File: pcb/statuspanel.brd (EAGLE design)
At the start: 57.1 x 66 mm, 5 parts

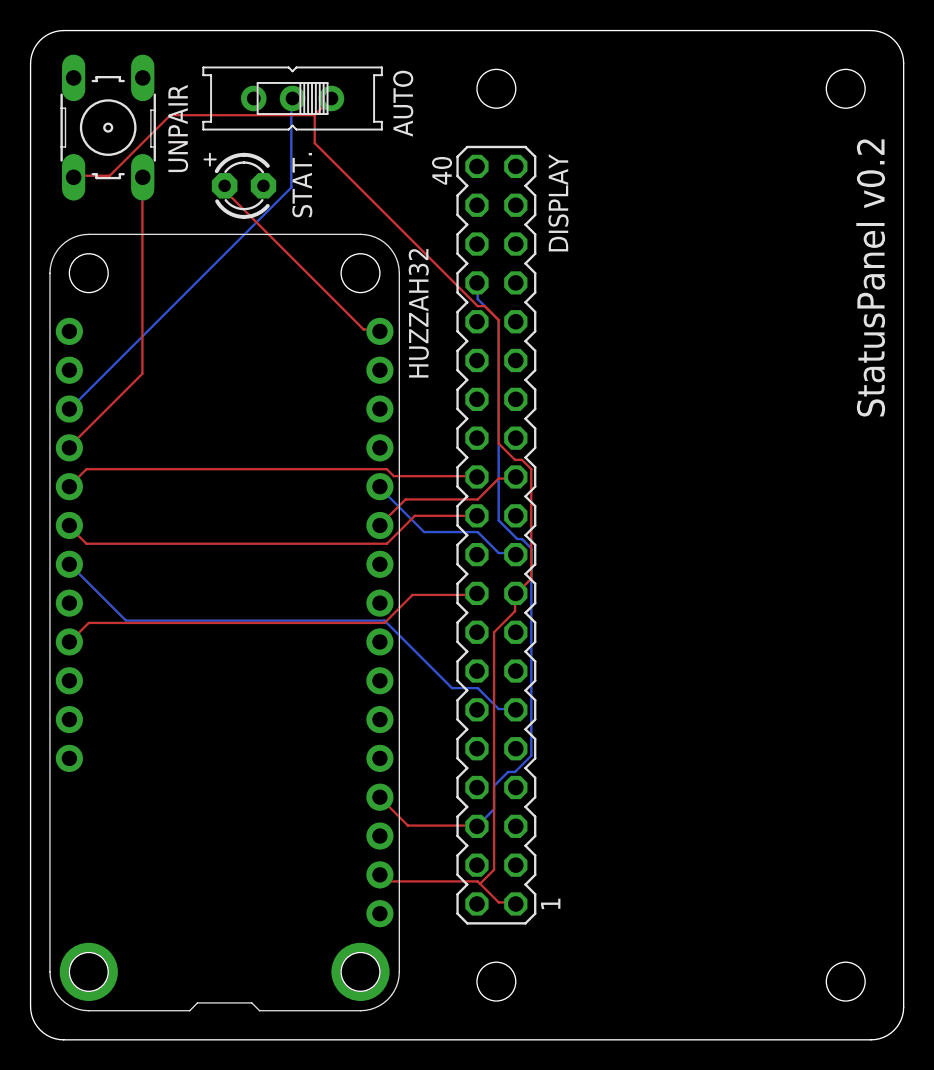
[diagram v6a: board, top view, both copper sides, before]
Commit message: Add the resistors to the board
- Divider
- Status LED
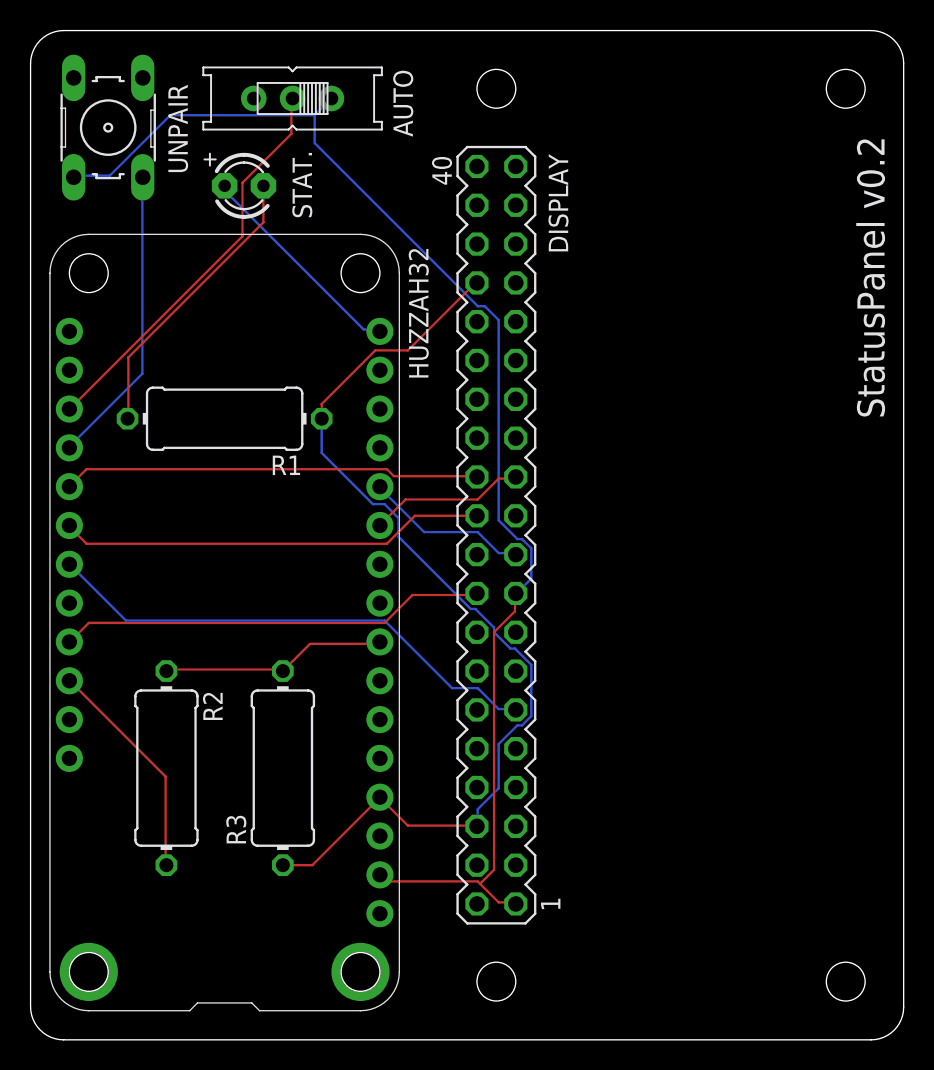
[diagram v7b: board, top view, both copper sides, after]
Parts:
- added R1: 5.1, adafruit:0411/12
- added R2, R3: 4.7K, adafruit:0411/12
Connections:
- new net USB: HUZZAH32.26, R2.2
- new net USBDETECT: HUZZAH32.8, R2.1, R3.2
- net GND: now also R1.1, R3.1
- net N$3: now also R1.2
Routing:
- net N$3: track 0.00 -> 18.9 mm
- net GND: track 46.1 -> 64.5 mm
- net USBDETECT: track 0.00 -> 14.9 mm
- net USB: track 0.00 -> 14.7 mm

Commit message: Update the PCB to tie 5V and 3V3 together to account for the new display controller board.
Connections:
- net 3V3: now also DISPLAY.2, DISPLAY.4
- net GND: now also DISPLAY.14, DISPLAY.20, DISPLAY.25, DISPLAY.30, DISPLAY.9
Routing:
- net GND: track 64.5 -> 81.1 mm
- net 3V3: track 86.8 -> 89.1 mm
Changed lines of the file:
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@@
 <?xml version="1.0" encoding="utf-8"?>
 <!DOCTYPE eagle SYSTEM "eagle.dtd">
-<eagle version="9.5.2">
+<eagle version="9.6.2">
 <drawing>
 <settings>
@@
 <wire x1="30.6324" y1="8.9916" x2="31.6992" y2="8.9916" width="0.1524" layer="1"/>
 <wire x1="29.2608" y1="10.3632" x2="29.4132" y2="10.2108" width="0.1524" layer="1"/>
-<wire x1="29.4132" y1="10.2108" x2="30.6324" y2="8.9916" width="0.1524" layer="1"/>
-<wire x1="23.1648" y1="10.3632" x2="29.2608" y2="10.3632" width="0.1524" layer="1"/>
+<wire x1="29.4132" y1="10.2108" x2="29.8704" y2="9.7536" width="0.1524" layer="1"/>
+<wire x1="29.8704" y1="9.7536" x2="30.6324" y2="8.9916" width="0.1524" layer="1"/>
+<wire x1="23.1648" y1="10.3632" x2="29.1084" y2="10.3632" width="0.1524" layer="1"/>
+<wire x1="29.1084" y1="10.3632" x2="29.2608" y2="10.3632" width="0.1524" layer="1"/>
 <wire x1="22.86" y1="10.668" x2="23.1648" y2="10.3632" width="0.1524" layer="1"/>
 <wire x1="31.6992" y1="8.9916" x2="31.75" y2="8.89" width="0.1524" layer="1"/>
@@
 <wire x1="31.8516" y1="29.2608" x2="32.766" y2="30.1752" width="0.1524" layer="16"/>
 <wire x1="31.8516" y1="29.2608" x2="31.75" y2="29.21" width="0.1524" layer="16"/>
+<contactref element="DISPLAY" pad="4"/>
+<contactref element="DISPLAY" pad="2"/>
+<wire x1="29.8704" y1="9.6012" x2="29.2608" y2="8.9916" width="0.1524" layer="1"/>
+<wire x1="29.8704" y1="9.7536" x2="29.8704" y2="9.6012" width="0.1524" layer="1"/>
+<wire x1="29.2608" y1="8.9916" x2="29.21" y2="8.89" width="0.1524" layer="1"/>
+<wire x1="29.1084" y1="11.43" x2="29.1084" y2="10.3632" width="0.1524" layer="1"/>
+<wire x1="29.1084" y1="11.43" x2="29.21" y2="11.43" width="0.1524" layer="1"/>
 </signal>
 <signal name="GND">
@@
 <wire x1="22.5552" y1="45.1104" x2="19.05" y2="41.6052" width="0.1524" layer="1"/>
 <wire x1="24.6888" y1="45.1104" x2="22.5552" y2="45.1104" width="0.1524" layer="1"/>
-<wire x1="29.1084" y1="49.53" x2="24.6888" y2="45.1104" width="0.1524" layer="1"/>
+<wire x1="29.1084" y1="49.53" x2="26.5176" y2="46.9392" width="0.1524" layer="1"/>
+<wire x1="26.5176" y1="46.9392" x2="24.6888" y2="45.1104" width="0.1524" layer="1"/>
 <wire x1="29.1084" y1="49.53" x2="29.21" y2="49.53" width="0.1524" layer="1"/>
 <wire x1="29.2608" y1="15.0876" x2="29.2608" y2="14.0208" width="0.1524" layer="16"/>
 <wire x1="30.6324" y1="16.4592" x2="29.2608" y2="15.0876" width="0.1524" layer="16"/>
-<wire x1="30.6324" y1="19.3548" x2="30.6324" y2="16.4592" width="0.1524" layer="16"/>
+<wire x1="30.6324" y1="19.3548" x2="30.6324" y2="19.05" width="0.1524" layer="16"/>
+<wire x1="30.6324" y1="19.05" x2="30.6324" y2="16.4592" width="0.1524" layer="16"/>
 <wire x1="31.8516" y1="20.574" x2="30.6324" y2="19.3548" width="0.1524" layer="16"/>
 <wire x1="32.1564" y1="20.574" x2="31.8516" y2="20.574" width="0.1524" layer="16"/>
@@
 <wire x1="31.6992" y1="25.6032" x2="32.766" y2="24.5364" width="0.1524" layer="16"/>
 <wire x1="31.3944" y1="25.6032" x2="31.6992" y2="25.6032" width="0.1524" layer="16"/>
-<wire x1="30.3276" y1="26.67" x2="31.3944" y2="25.6032" width="0.1524" layer="16"/>
+<wire x1="30.3276" y1="26.67" x2="30.9372" y2="26.0604" width="0.1524" layer="16"/>
+<wire x1="30.9372" y1="26.0604" x2="31.3944" y2="25.6032" width="0.1524" layer="16"/>
 <wire x1="30.3276" y1="26.9748" x2="30.3276" y2="26.67" width="0.1524" layer="16"/>
 <wire x1="29.1084" y1="28.194" x2="30.3276" y2="26.9748" width="0.1524" layer="16"/>
 <wire x1="28.8036" y1="28.194" x2="29.1084" y2="28.194" width="0.1524" layer="16"/>
-<wire x1="24.0792" y1="32.9184" x2="28.8036" y2="28.194" width="0.1524" layer="16"/>
+<wire x1="24.0792" y1="32.9184" x2="27.1272" y2="29.8704" width="0.1524" layer="16"/>
+<wire x1="27.1272" y1="29.8704" x2="28.8036" y2="28.194" width="0.1524" layer="16"/>
 <wire x1="24.0792" y1="34.1376" x2="24.0792" y2="32.9184" width="0.1524" layer="16"/>
 <wire x1="23.1648" y1="35.052" x2="24.0792" y2="34.1376" width="0.1524" layer="16"/>
@@
 <wire x1="19.05" y1="40.64" x2="19.05" y2="38.4048" width="0.1524" layer="16"/>
 <wire x1="29.2608" y1="14.0208" x2="29.21" y2="13.97" width="0.1524" layer="16"/>
+<contactref element="DISPLAY" pad="30"/>
+<wire x1="26.67" y1="46.9392" x2="29.1084" y2="44.5008" width="0.1524" layer="1"/>
+<wire x1="26.5176" y1="46.9392" x2="26.67" y2="46.9392" width="0.1524" layer="1"/>
+<wire x1="29.1084" y1="44.5008" x2="29.21" y2="44.45" width="0.1524" layer="1"/>
+<contactref element="DISPLAY" pad="20"/>
+<contactref element="DISPLAY" pad="14"/>
+<wire x1="30.9372" y1="25.908" x2="29.2608" y2="24.2316" width="0.1524" layer="16"/>
+<wire x1="30.9372" y1="26.0604" x2="30.9372" y2="25.908" width="0.1524" layer="16"/>
+<wire x1="29.2608" y1="24.2316" x2="29.21" y2="24.13" width="0.1524" layer="16"/>
+<wire x1="29.1084" y1="31.8516" x2="27.1272" y2="29.8704" width="0.1524" layer="16"/>
+<wire x1="29.1084" y1="31.8516" x2="29.21" y2="31.75" width="0.1524" layer="16"/>
+<contactref element="DISPLAY" pad="9"/>
+<contactref element="DISPLAY" pad="25"/>
+<wire x1="30.6324" y1="19.05" x2="31.75" y2="19.05" width="0.1524" layer="16"/>
+<wire x1="29.2608" y1="43.2816" x2="29.2608" y2="44.3484" width="0.1524" layer="1"/>
+<wire x1="30.6324" y1="41.91" x2="29.2608" y2="43.2816" width="0.1524" layer="1"/>
+<wire x1="30.6324" y1="40.5384" x2="30.6324" y2="41.91" width="0.1524" layer="1"/>
+<wire x1="31.6992" y1="39.4716" x2="30.6324" y2="40.5384" width="0.1524" layer="1"/>
+<wire x1="29.2608" y1="44.3484" x2="29.21" y2="44.45" width="0.1524" layer="1"/>
+<wire x1="31.6992" y1="39.4716" x2="31.75" y2="39.37" width="0.1524" layer="1"/>
 </signal>
 <signal name="AUTO">
